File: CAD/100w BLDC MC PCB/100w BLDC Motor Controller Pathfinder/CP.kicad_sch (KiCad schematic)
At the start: 4 parts, among them J1 USB_C_Receptacle_USB2.0, U3 USBLC6-2SC6

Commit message: poquito a poquito
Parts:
- added U7: MCP2542FD-E/MF, DFN8_3x3MC_MCH, symbol 2024-02-01_06-55-44:MCP2542FD-E_MF
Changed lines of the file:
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@@
+    )
+  )
+  (symbol (lib_id "2024-02-01_06-55-44:MCP2542FD-E_MF") (at 22.86 106.045 0) (unit 1)
+    (in_bom yes) (on_board yes) (dnp no)
+    (property "Reference" "U7" (at 51.435 99.695 0)
+      (effects (font (size 1.524 1.524)))
+    )
+    (property "Value" "MCP2542FD-E/MF" (at 41.91 120.015 0)
+      (effects (font (size 1.524 1.524)))
+    )
+    (property "Footprint" "DFN8_3x3MC_MCH" (at 21.59 103.505 0)
+      (effects (font (size 1.27 1.27) italic) hide)
+    )
+    (property "Datasheet" "MCP2542FD-E/MF" (at 21.59 100.965 0)
+      (effects (font (size 1.27 1.27) italic) hide)
+    )
+    (pin "1")
+    (pin "2")
+    (pin "3")
+    (pin "4")
+    (pin "5")
+    (pin "6")
+    (pin "7")
+    (pin "8")
+    (pin "9")
+    (instances
+      (project "100w BLDC Motor Controller Pathfinder"
+        (path "/bd5e620c-77b3-46f1-a718-89cd1182fd75/ea8134e5-754c-408f-918e-72ebb0e84e8d"
+          (reference "U7") (unit 1)
+        )
+      )
     )
   )

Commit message: aun no
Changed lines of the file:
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@@
     (effects (font (size 1.27 1.27)) (justify left bottom))
   )
-  (label "USB_D-" (at 85.725 33.655 0) (fields_autoplaced)
-    (effects (font (size 1.27 1.27)) (justify left bottom))
+  (global_label "USB_D-" (shape input) (at 85.725 33.655 0) (fields_autoplaced)
+    (effects (font (size 1.27 1.27)) (justify left))
+    (property "Intersheetrefs" "${INTERSHEET_REFS}" (at 96.2508 33.655 0)
+      (effects (font (size 1.27 1.27)) (justify left) hide)
+    )
   )
-  (label "USB_D+" (at 83.82 55.88 0) (fields_autoplaced)
-    (effects (font (size 1.27 1.27)) (justify left bottom))
+  (global_label "USB_D+" (shape input) (at 83.82 55.88 0) (fields_autoplaced)
+    (effects (font (size 1.27 1.27)) (justify left))
+    (property "Intersheetrefs" "${INTERSHEET_REFS}" (at 94.3458 55.88 0)
+      (effects (font (size 1.27 1.27)) (justify left) hide)
+    )
   )
   (symbol (lib_id "power:VBUS") (at 90.805 26.67 0) (unit 1)

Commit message: Errores pero que probablemente no son errores
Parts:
- removed U7: MCP2542FD-E/MF, DFN8_3x3MC_MCH, symbol 2024-02-01_06-55-44:MCP2542FD-E_MF
- added C2 (x2): 100n, symbol Device:C
- added J2, J3: 15-91-2025, CONN2_15-91-2025_MOL, symbol 2024-02-05_06-15-11:15-91-2025
- added J4, J5, J6, J7: Conn_01x03_Pin, Connector_Harwin:Harwin_M20-89003xx_1x03_P2.54mm_Horizontal, symbol Connector:Conn_01x03_Pin
- added R12: 120, symbol Device:R
- added S1: JS202011SCQN, digikey-footprints:Switch_Slide_JS202011SCQN, symbol dk_Slide-Switches:JS202011SCQN
- added U8: PTCAN3413DRBR, VSON8-DRB_TEX, symbol 2024-02-05_02-01-50:PTCAN3413DRBR
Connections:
- net GND: now also C2.2, C2.2, J4.2 (Pin_2), J5.3 (Pin_3), J6.3 (Pin_3), J7.3 (Pin_3), U8.2 (GND), U8.8 (STB), U8.9 (THERMAL_PAD)
- new net: J2.1, J3.1, S1.2, U8.7 (CANH)
- new net: J2.2, J3.2, R12.2, U8.6 (CANL)
- new net: R12.1, S1.3
- new net +3V3: C2.1, C2.1, J5.2 (Pin_2), J6.2 (Pin_2), J7.2 (Pin_2), U8.3 (VCC), U8.5 (VIO)
- new net CAN_RX: U8.4 (RXD)
- new net CAN_TX: U8.1 (TXD)
- new net GPIO10: J5.1 (Pin_1)
- new net GPIO24: J6.1 (Pin_1)
- new net GPIO25: J7.1 (Pin_1)
- new net SWCLK: J4.1 (Pin_1)
- new net SWDIO: J4.3 (Pin_3)
- no-connect marks 2 -> 6
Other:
- note added: "CAN BUS"
- note added: "Debug - SWD"
- note added: "GPIO Extra"
- moved on the sheet: J1, R6, R7, U3

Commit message: Rev: 0.1
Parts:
- added J10: Conn_01x03_Pin, Connector_Harwin:Harwin_M20-89003xx_1x03_P2.54mm_Horizontal, symbol Connector:Conn_01x03_Pin
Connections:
- net GND: now also J10.3 (Pin_3)
- net GPIO10 renamed GPIO23
- new net UART_RX: J10.2 (Pin_2)
- new net UART_TX: J10.1 (Pin_1)
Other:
- note added: "UART 1"
- company: (none) -> SCS
- title: (none) -> 100w BLDC Motor Controller Pathfinder
- moved on the sheet: C2, J1, J2, J3, J4, J5, J6, J7, R12, R6, R7, S1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

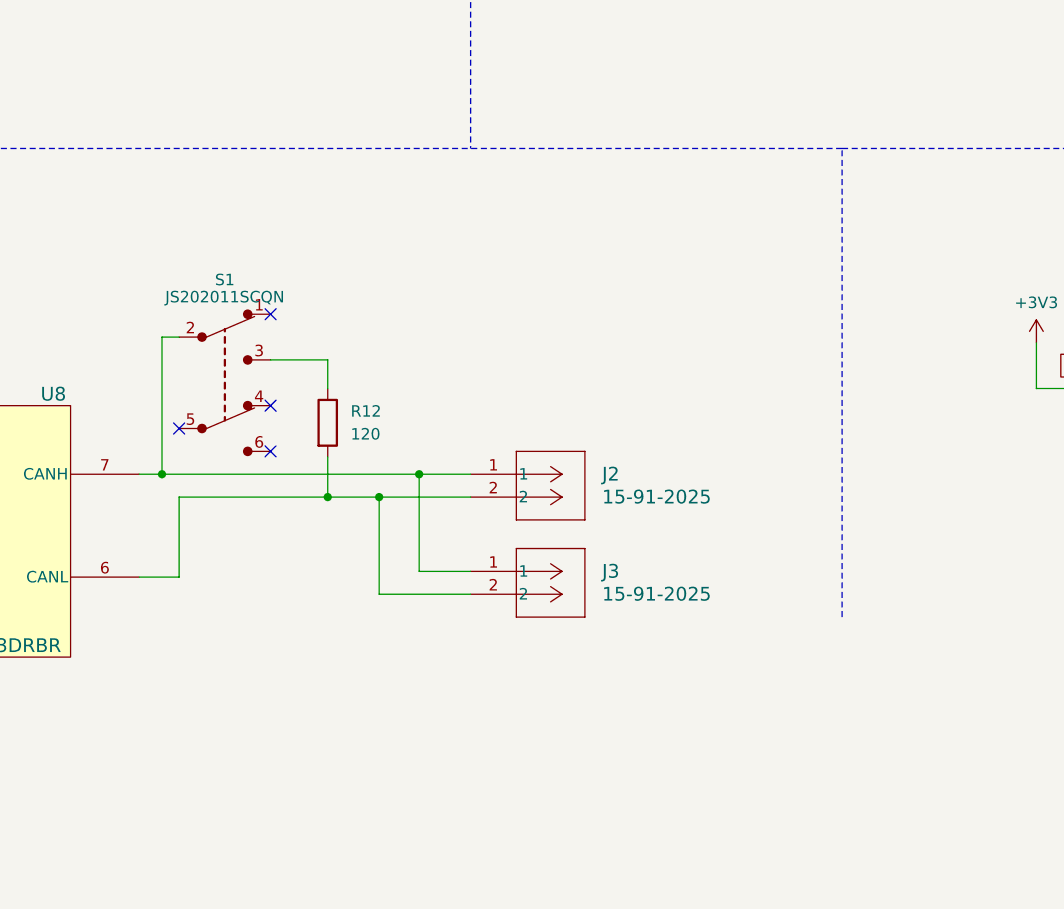
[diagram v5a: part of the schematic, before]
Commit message: CAN bus Upgrades
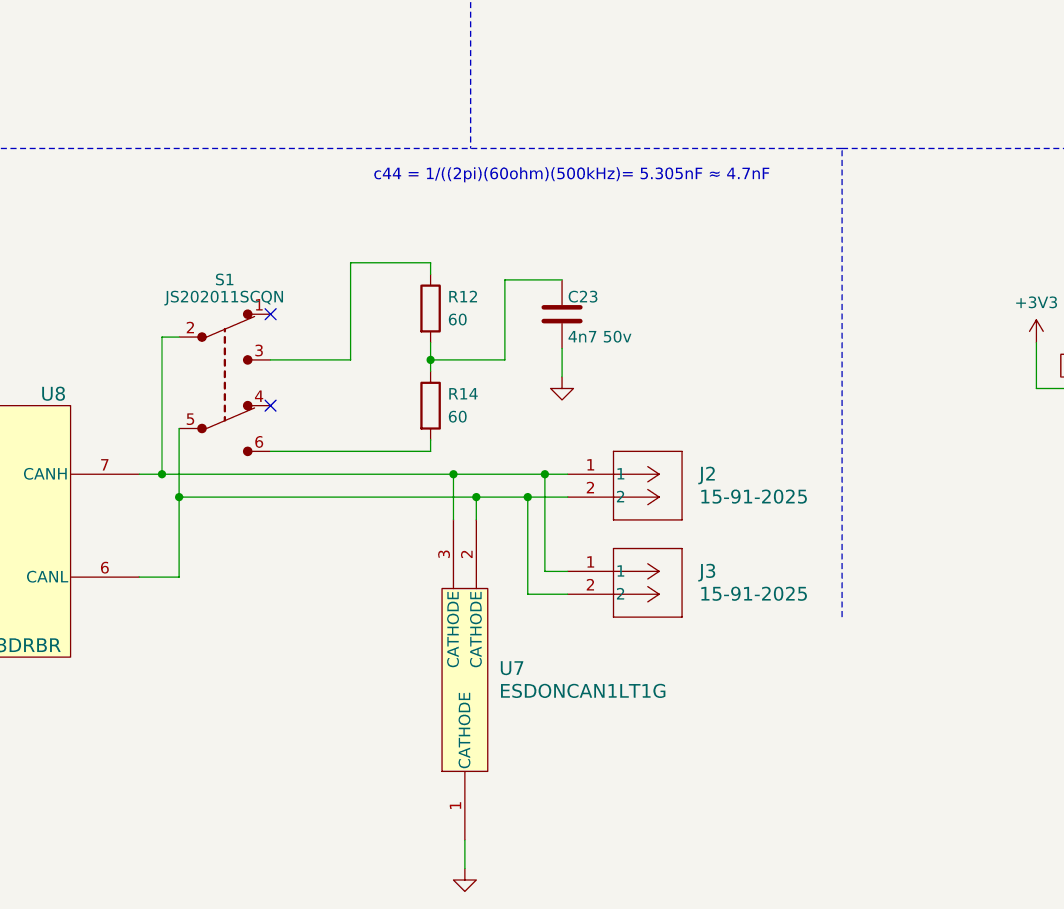
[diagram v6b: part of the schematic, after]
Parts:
- added C23: 4n7 50v, symbol Device:C
- added R14: 60, symbol Device:R
- added U7: ESDONCAN1LT1G, SOT-23-3_1P4X3P040_ONS, symbol 2024-02-07_03-49-28:ESDONCAN1LT1G
- R12: value 120 -> 60
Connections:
- net GND: now also C23.2, U7.1 (CATHODE)
- net at J2.1, J3.1, S1.2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: now also U7.3 (CATHODE)
- net at J2.2, J3.2, U8.6 (CANL): now also S1.5, U7.2 (CATHODE); no longer R12.2
- net at S1.6: now also R14.2
- new net: C23.1, R12.2, R14.1
- no-connect marks 6 -> 4
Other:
- note added: "c44 = 1/((2pi)(60ohm)(500kHz)= 5.305nF ≈ 4.7nF"
- moved on the sheet: J2, J3
